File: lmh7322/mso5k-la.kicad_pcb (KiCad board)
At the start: 4 copper layers, 84.5 x 90.9 mm, 208 parts, among them J101 output, J102 input, U201 lmh7322, U301 lmh7322, U401 lmh7322, U501 lmh7322, U601 lmh7322, U701 lmh7322, U801 lmh7322, U901 lmh7322

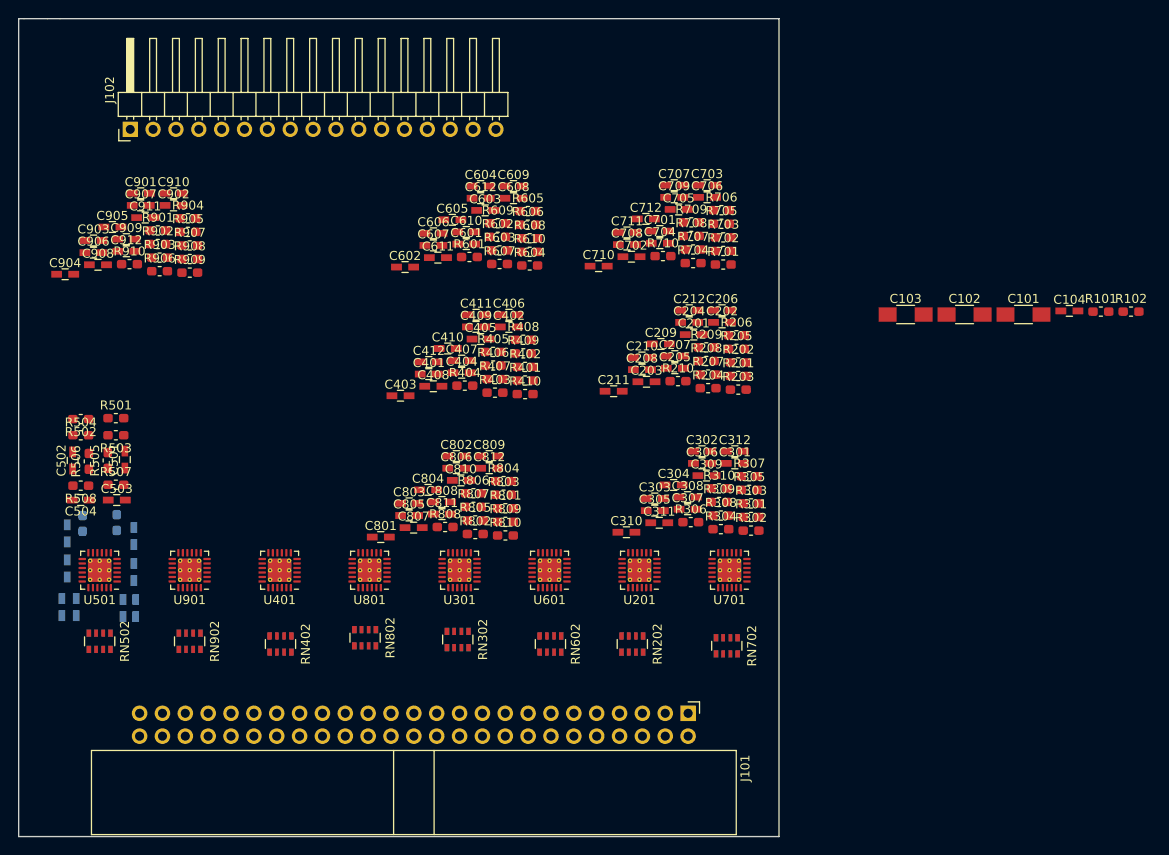
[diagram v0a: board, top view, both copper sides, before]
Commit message: Finished the 4-layer single-sided board
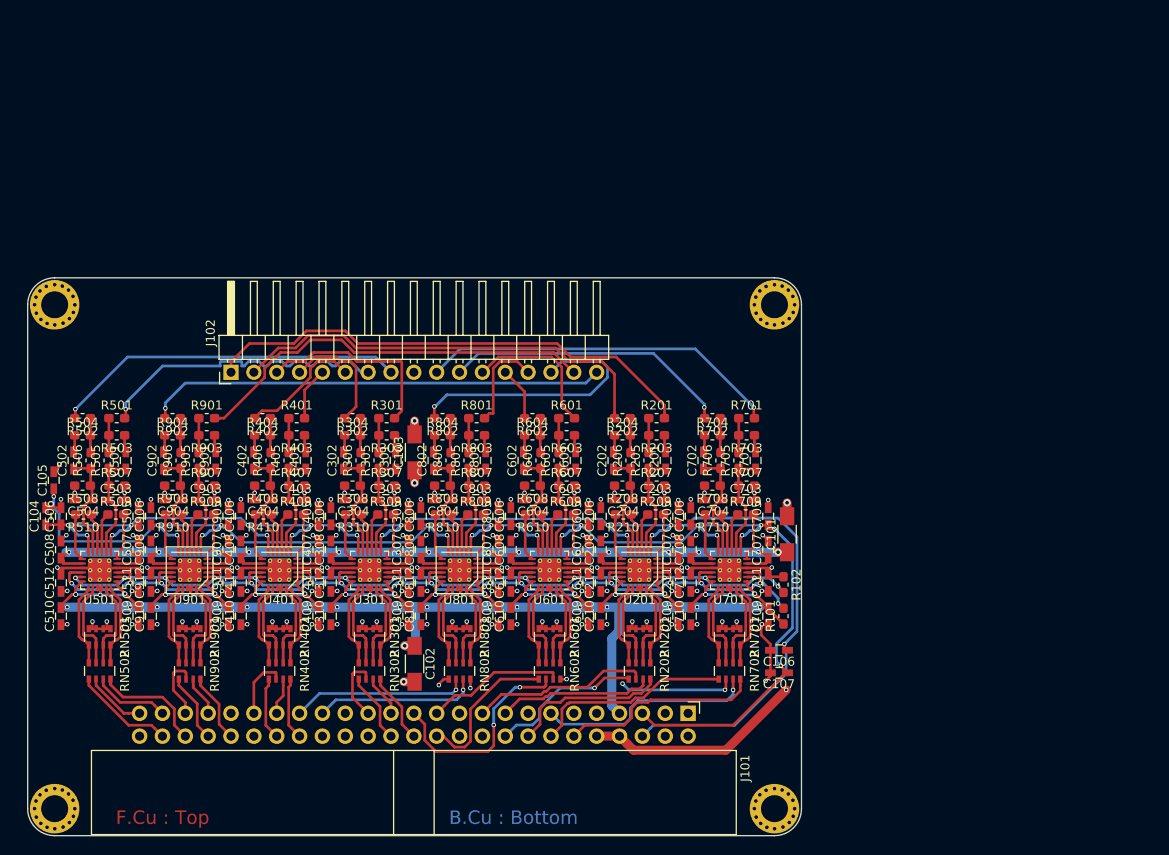
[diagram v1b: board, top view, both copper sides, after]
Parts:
- added C105: 100n, Capacitors_SMD.pretty:C_0603_HandSoldering, F.Cu at (44.9, 135.5)
- added C106: 100n, Capacitors_SMD.pretty:C_0603_HandSoldering, F.Cu at (125.5, 154.4)
- added C107: 100n, Capacitors_SMD.pretty:C_0603_HandSoldering, F.Cu at (125.5, 156.9)
- added TP101: 3mm, lmh7322:3mm, F.Cu at (45.0, 116.0)
- added TP102: 3mm, lmh7322:3mm, F.Cu at (45.0, 172.0)
- added TP103: 3mm, lmh7322:3mm, F.Cu at (125.0, 116.0)
- added TP104: 3mm, lmh7322:3mm, F.Cu at (125.0, 172.0)
- C505, C506, C507, C508, C509, C510, C511, C512, R509, R510, RN201, RN301, RN401, RN501, RN601, RN701, RN801, RN901: moved to F.Cu
- moved C104 116.0 mm to (44.0, 139.5), turned to 90 degrees
- moved C102 72.4 mm to (85.0, 155.9), turned to 270 degrees
- moved C103 56.7 mm to (85.0, 132.4), turned to 90 degrees
- moved R102 49.1 mm to (126.0, 147.1), turned to 270 degrees
- moved R101 48.9 mm to (126.0, 150.6), turned to 90 degrees
- moved C609 48.5 mm to (104.3, 150.6), turned to 90 degrees
- moved C709 47.7 mm to (124.3, 150.6), turned to 90 degrees
- moved C312 47.2 mm to (75.7, 146.9), turned to 90 degrees
- moved C910 47.1 mm to (55.7, 150.6), turned to 90 degrees
- moved R302 46.0 mm to (78.1, 128.6), turned to 180 degrees
- moved C909 43.4 mm to (64.3, 150.6), turned to 90 degrees
- moved C610 43.0 mm to (95.7, 150.6), turned to 90 degrees
- moved C612 42.9 mm to (95.7, 146.9), turned to 90 degrees
- moved R304 42.3 mm to (78.1, 130.5)
- moved C711 42.0 mm to (124.3, 146.9), turned to 90 degrees
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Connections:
- C104 pad 1: (no net) -> Vref_0-7
- U201 pad 25: (no net) -> -2V5
- U301 pad 25: (no net) -> -2V5
- U401 pad 25: (no net) -> -2V5
- U501 pad 25: (no net) -> -2V5
- U601 pad 25: (no net) -> -2V5
- U701 pad 25: (no net) -> -2V5
- U801 pad 25: (no net) -> -2V5
- U901 pad 25: (no net) -> -2V5
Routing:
- net GND: track 0.00 -> 642.2 mm, vias 0 -> 101
- net +2V5: track 0.00 -> 234.5 mm, vias 0 -> 49
- net -2V5: track 0.00 -> 222.2 mm, vias 0 -> 17
- net +4V: track 0.00 -> 191.8 mm, vias 0 -> 18
- net Vref_8-15: track 0.00 -> 169.0 mm, vias 0 -> 19
- net Vref_0-7: track 0.00 -> 164.2 mm, vias 0 -> 17
- net ~LE: track 0.00 -> 132.0 mm, vias 0 -> 17
- net LE: track 0.00 -> 103.6 mm, vias 0 -> 17
- net In0: track 0.00 -> 55.6 mm
- net In15: track 0.00 -> 51.1 mm, vias 0 -> 1
- net In1: track 0.00 -> 48.5 mm
- net In14: track 0.00 -> 45.6 mm
- net In8: track 0.00 -> 40.2 mm, vias 0 -> 1
- net In7: track 0.00 -> 39.2 mm, vias 0 -> 1
- net In6: track 0.00 -> 33.7 mm, vias 0 -> 1
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- added copper zone on 3_Power, net -2V5
- added copper zone on 2_Ground, net GND
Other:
- board size 84.5 x 90.9 mm -> 86 x 62 mm
- board text added: "2 Ground"
- board text added: "3 Power"
- board text added: "B.Cu : Bottom"
- board text added: "F.Cu : Top"
